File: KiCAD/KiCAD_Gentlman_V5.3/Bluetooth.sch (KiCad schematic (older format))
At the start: 16 parts, among them J7 PinHeader2.54mm_6, U7 nRF52832-QFAA, U8 nRF52832_DM-SModule, Y1 Y_32MHz

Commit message: KSG : 반이중통신용 회로도 구성 완료
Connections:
- net STM32_UART_TX is gone; now on net STM32_UART: J7.6 (Pin_6), U7.15 (P0.12), U8.22 (P0.12)
- net STM32_UART_RX renamed STM32_UART
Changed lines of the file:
@@
 	2300 3550 2050 3550
 Connection ~ 2300 3550
-Text GLabel 2200 4150 0    50   Input ~ 0
-nRF_SWCLK
 Wire Wire Line
 	2200 4150 3250 4150
-Text GLabel 2200 4250 0    50   Input ~ 0
+Text GLabel 2200 4250 0    50   BiDi ~ 0
 nRF_SWDIO
 Wire Wire Line
 	2200 4250 3250 4250
-Text GLabel 2200 4350 0    50   Input ~ 0
+Text GLabel 2200 4350 0    50   Output ~ 0
 nRF_UART_TX
 Wire Wire Line
@@
 	7100 2650 7500 2650
 Wire Wire Line
-	1300 7350 1450 7350
-Text GLabel 1450 7350 2    50   Input ~ 0
+	2450 6850 2750 6850
+Text GLabel 2750 6850 2    50   Input ~ 0
 DEC4
-NoConn ~ 1300 7350
+NoConn ~ 2450 6850
 NoConn ~ 5050 2350
 NoConn ~ 5050 2450
@@
 Wire Wire Line
 	1650 1650 2150 1650
-Text GLabel 2350 7050 2    50   Output ~ 0
+Text GLabel 2750 6550 2    50   Input ~ 0
 nRF_UART_TX
-Text GLabel 2350 7150 2    50   Output ~ 0
+Text GLabel 2750 6650 2    50   Output ~ 0
 nRF_UART_RX
-Text GLabel 1700 7150 0    50   Output ~ 0
-STM32_UART_TX
-Text GLabel 1700 7050 0    50   Output ~ 0
-STM32_UART_RX
-Wire Wire Line
-	1700 7050 2350 7050
-Wire Wire Line
-	1700 7150 2350 7150
+Text GLabel 2450 6550 0    50   BiDi ~ 0
+STM32_UART
+Wire Wire Line
+	2450 6550 2600 6550
+Text GLabel 2200 4150 0    50   Input ~ 0
+nRF_SWCLK
+Wire Wire Line
+	2600 6550 2600 6650
+Connection ~ 2600 6550
+Wire Wire Line
+	2600 6550 2750 6550
+Wire Wire Line
+	2600 6650 2750 6650
 $EndSCHEMATC

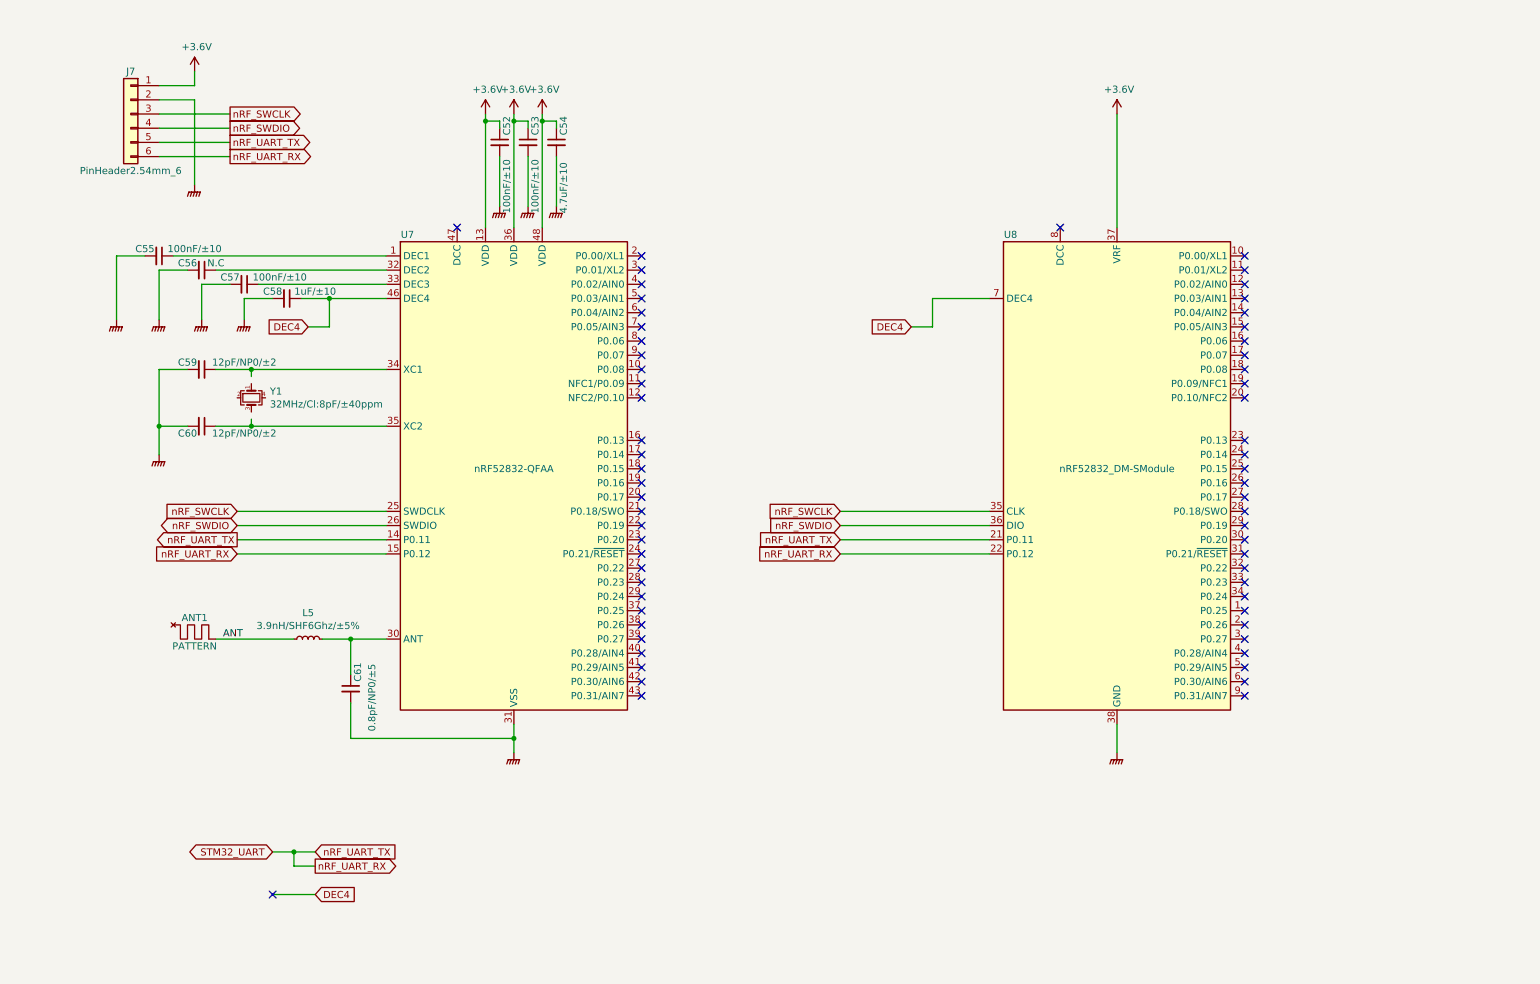
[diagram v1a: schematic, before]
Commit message: KSG : 회로도 에 nRF52 DC-DC 레귤레이터 추가
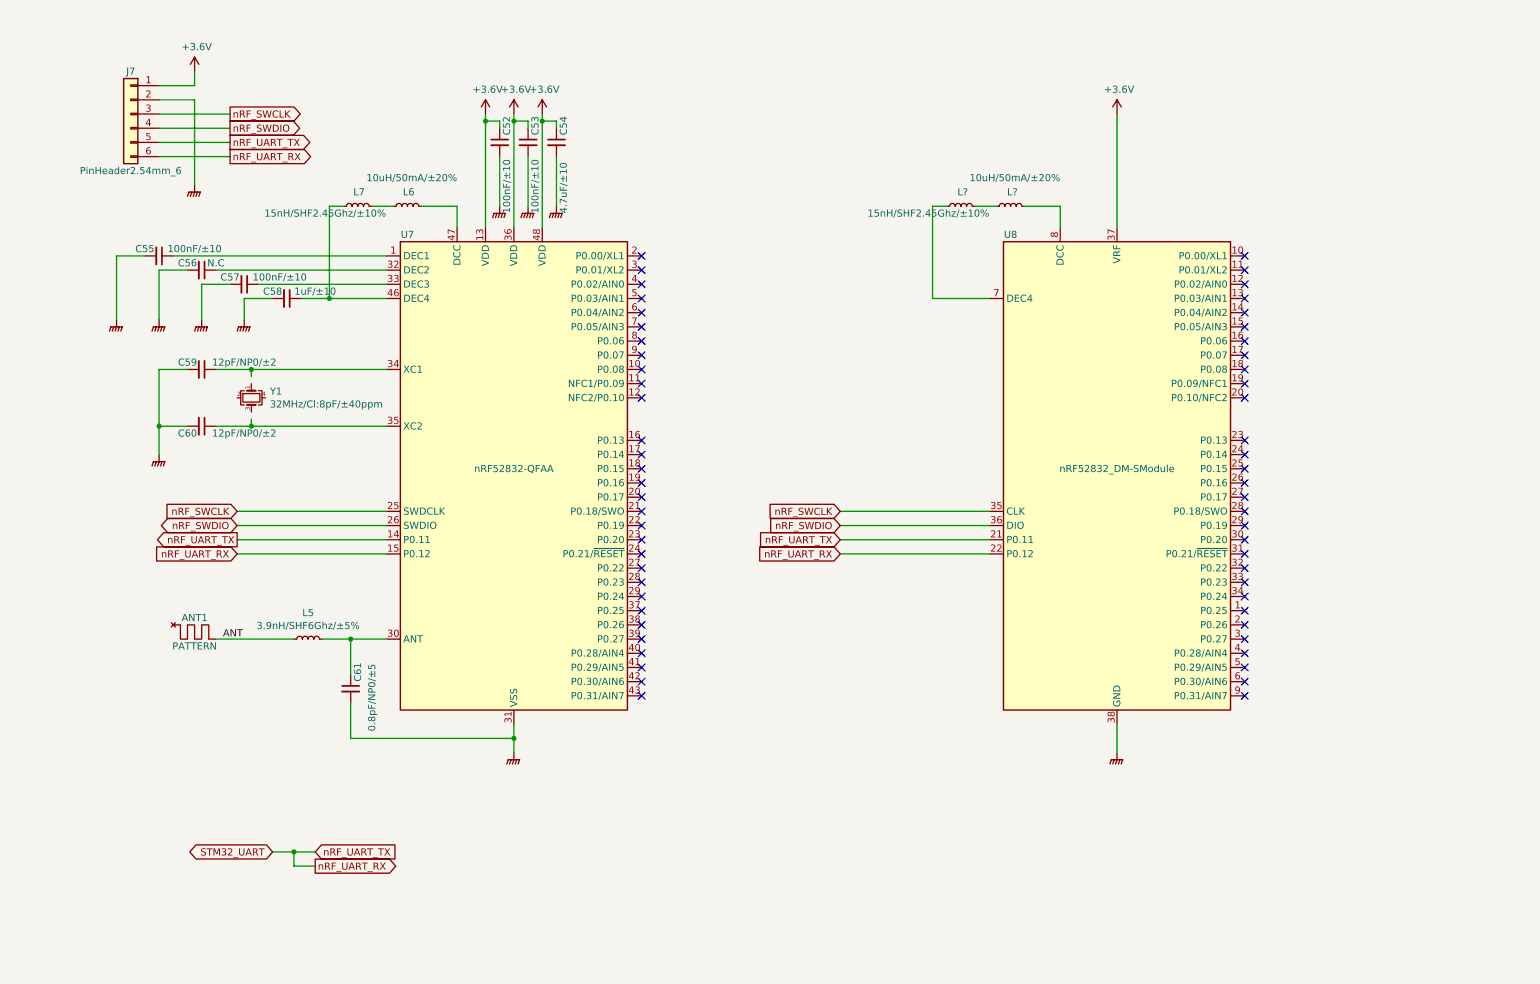
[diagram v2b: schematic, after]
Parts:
- added L6, L?: L_10uH, Custom:L_0603_1608Metric, symbol Custom:L_10uH
- added L7, L?: L_15nH, Custom:L_01005_0402Metric, symbol Custom:L_15nH
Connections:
- net at U7.47 (DCC): now also L6.2
- net at U8.8 (DCC): now also L?.2
- net DEC4: no longer names the net of C58.1, U7.46 (DEC4)
- net DEC4: now also L7.1; no longer U8.7 (DEC4)
- new net: L6.1, L7.2
- new net: L?.1, U8.7 (DEC4)
- new net: L?.1, L?.2
- no-connect marks 63 -> 60
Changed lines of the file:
@@
 Wire Wire Line
 	2250 2650 2450 2650
-Wire Wire Line
-	2650 2650 2850 2650
-Wire Wire Line
-	2850 2650 2850 2850
-Wire Wire Line
-	2850 2850 2700 2850
-Text GLabel 2700 2850 0    50   Input ~ 0
-DEC4
-Connection ~ 2850 2650
-Wire Wire Line
-	2850 2650 3250 2650
 $Comp
 L Custom:Y_32MHz Y1
@@
 Wire Wire Line
 	8400 1350 8400 2150
-NoConn ~ 8000 2150
-NoConn ~ 3750 2150
-Wire Wire Line
-	7100 2650 7100 2850
-Wire Wire Line
-	7100 2850 6950 2850
-Text GLabel 6950 2850 0    50   Input ~ 0
-DEC4
-Wire Wire Line
-	7100 2650 7500 2650
-Wire Wire Line
-	2450 6850 2750 6850
-Text GLabel 2750 6850 2    50   Input ~ 0
-DEC4
-NoConn ~ 2450 6850
 NoConn ~ 5050 2350
 NoConn ~ 5050 2450
@@
 Wire Wire Line
 	2600 6650 2750 6650
+$Comp
+L Custom:L_15nH L7
+U 1 1 61A0ACB5
+P 3050 2000
+F 0 "L7" V 3150 1950 50  0000 L CNN
+F 1 "L_15nH" H 3080 1960 50  0001 L CNN
+F 2 "Custom:L_01005_0402Metric" H 3050 2000 50  0001 C CNN
+F 3 ".\\Dataseets\\jti-cat-rf-ind-844822.pdf" H 3050 2000 50  0001 C CNN
+F 4 "15nH/SHF2.45Ghz/±10%" V 3000 1800 50  0000 L CNN "Field4"
+F 5 "SMD INDUCTOR" H 3050 2000 50  0001 C CNN "Description"
+F 6 "15nH/SHF21Ghz/±10%" H 3050 2000 50  0001 C CNN "Comment"
+F 7 "1005" H 3050 2000 50  0001 C CNN "TYPE"
+F 8 "JOHANSON" H 3050 2000 50  0001 C CNN "MAKER"
+F 9 "L-07C15NKV6T" H 3050 2000 50  0001 C CNN "PartName"
+F 10 "https://kr.mouser.com/ProductDetail/Johanson/L-07C15NKV6T?qs=sGAEpiMZZMsjJi7B1kCaqYmWy2J2VjPA6p6zKg5MyIw%3D" H 3050 2000 50  0001 C CNN "Shop"
+	1    3050 2000
+	0    -1   -1   0
+$EndComp
+$Comp
+L Custom:L_10uH L6
+U 1 1 61A09931
+P 3400 2000
+F 0 "L6" V 3500 1950 50  0000 L CNN
+F 1 "L_10uH" H 3430 1960 50  0001 L CNN
+F 2 "Custom:L_0603_1608Metric" H 3400 2000 50  0001 C CNN
+F 3 ".\\Dataseets\\JELF243B_0012-1633801.pdf" H 3400 2000 50  0001 C CNN
+F 4 "10uH/50mA/±20%" V 3600 1650 50  0000 L CNN "Field4"
+F 5 "SMD INDUCTOR" H 3400 2000 50  0001 C CNN "Description"
+F 6 "10uH/50mA/±20%" H 3400 2000 50  0001 C CNN "Comment"
+F 7 "0603" H 3400 2000 50  0001 C CNN "TYPE"
+F 8 "MURATA" H 3400 2000 50  0001 C CNN "MAKER"
+F 9 "LQM18FN100M00D" H 3400 2000 50  0001 C CNN "PartName"
+F 10 "https://kr.mouser.com/ProductDetail/Murata/LQM18FN100M00D?qs=sGAEpiMZZMvxX9Q80wbhCb2WlNhDJeZC" H 3400 2000 50  0001 C CNN "Shop"
+	1    3400 2000
+	0    -1   -1   0
+$EndComp
+Wire Wire Line
+	2950 2000 2850 2000
+Wire Wire Line
+	3150 2000 3300 2000
+Wire Wire Line
+	3500 2000 3750 2000
+Wire Wire Line
+	3750 2000 3750 2150
+Wire Wire Line
+	2650 2650 2850 2650
+Wire Wire Line
+	2850 2000 2850 2650
+Connection ~ 2850 2650
+Wire Wire Line
+	2850 2650 3250 2650
+$Comp
+L Custom:L_15nH L?
+U 1 1 61A6256C
+P 7300 2000
+F 0 "L?" V 7400 1950 50  0000 L CNN
+F 1 "L_15nH" H 7330 1960 50  0001 L CNN
+F 2 "Custom:L_01005_0402Metric" H 7300 2000 50  0001 C CNN
+F 3 ".\\Dataseets\\jti-cat-rf-ind-844822.pdf" H 7300 2000 50  0001 C CNN
+F 4 "15nH/SHF2.45Ghz/±10%" V 7250 1800 50  0000 L CNN "Field4"
+F 5 "SMD INDUCTOR" H 7300 2000 50  0001 C CNN "Description"
+F 6 "15nH/SHF21Ghz/±10%" H 7300 2000 50  0001 C CNN "Comment"
+F 7 "1005" H 7300 2000 50  0001 C CNN "TYPE"
+F 8 "JOHANSON" H 7300 2000 50  0001 C CNN "MAKER"
+F 9 "L-07C15NKV6T" H 7300 2000 50  0001 C CNN "PartName"
+F 10 "https://kr.mouser.com/ProductDetail/Johanson/L-07C15NKV6T?qs=sGAEpiMZZMsjJi7B1kCaqYmWy2J2VjPA6p6zKg5MyIw%3D" H 7300 2000 50  0001 C CNN "Shop"
+	1    7300 2000
+	0    -1   -1   0
+$EndComp
+$Comp
+L Custom:L_10uH L?
+U 1 1 61A62579
+P 7650 2000
+F 0 "L?" V 7750 1950 50  0000 L CNN
+F 1 "L_10uH" H 7680 1960 50  0001 L CNN
+F 2 "Custom:L_0603_1608Metric" H 7650 2000 50  0001 C CNN
+F 3 ".\\Dataseets\\JELF243B_0012-1633801.pdf" H 7650 2000 50  0001 C CNN
+F 4 "10uH/50mA/±20%" V 7850 1650 50  0000 L CNN "Field4"
+F 5 "SMD INDUCTOR" H 7650 2000 50  0001 C CNN "Description"
+F 6 "10uH/50mA/±20%" H 7650 2000 50  0001 C CNN "Comment"
+F 7 "0603" H 7650 2000 50  0001 C CNN "TYPE"
+F 8 "MURATA" H 7650 2000 50  0001 C CNN "MAKER"
+F 9 "LQM18FN100M00D" H 7650 2000 50  0001 C CNN "PartName"
+F 10 "https://kr.mouser.com/ProductDetail/Murata/LQM18FN100M00D?qs=sGAEpiMZZMvxX9Q80wbhCb2WlNhDJeZC" H 7650 2000 50  0001 C CNN "Shop"
+	1    7650 2000
+	0    -1   -1   0
+$EndComp
+Wire Wire Line
+	7200 2000 7100 2000
+Wire Wire Line
+	7400 2000 7550 2000
+Wire Wire Line
+	7750 2000 8000 2000
+Wire Wire Line
+	8000 2000 8000 2150
+Wire Wire Line
+	7100 2000 7100 2650
+Wire Wire Line
+	7100 2650 7500 2650
 $EndSCHEMATC

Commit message: KSG : V5.3B용으로 회로도 수정 및 PCB 아트웤 완료.(샘플PCB주문됨)
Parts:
- added JP1, JP2, JP3: PinHeader2.54mm-2-Jumper, Custom:PinHeader_1x02_P2.54mm_Vertical, symbol Custom:PinHeader2.54mm-2-Jumper
- added L10: L_10uH, Custom:L_0603_1608Metric, symbol Custom:L_10uH
- added L11: L_15nH, Custom:L_0402_1005Metric, symbol Custom:L_15nH
- added U9: nRF52810_PLE52M, Custom:nRF52810_PLE52M, symbol Custom:nRF52810_PLE52M
- ANT1: symbol Custom:ANT -> Custom:PATTERN_ANT; Field4 PATTERN -> (none)
- C52, C53, C55, C57: Comment 100nF/±10 -> (none); Description CHIP CERAMIC CAP -> (none); Field4 100nF/±10 -> (none); MAKER MURATA ELECTRONICS -> (none); Maker (none) -> SAMSUNG ELECTRO-MECHANICS; PartName GRM155R61H104KE14D -> 100nF/±10; Replacement (none) -> CL05A104KA5NNNC; Shop https://kr.mouser.com/ProductDetail/Murata/GRM155R61H104KE1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 -> https://www.eleparts.co.kr/goods/view?no=8011439; TYPE 1005 -> (none); Type (none) -> CHIP CERAMIC CAP
- C54: Comment 4.7uF/±10 -> (none); Description CHIP CERAMIC CAP -> (none); Field4 4.7uF/±10 -> (none); MAKER SAMSUNG ELECTRO-MECHANICS -> (none); Maker (none) -> SAMSUNG ELECTRO-MECHANICS; PartName CL05A475KQ5NRNC -> 4.7uF/±10; Replacement (none) -> CL05A475KP5NRNC; Shop https://kr.mouser.com/ProductDetail/Samsung-Electro-Mechani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 -> https://www.eleparts.co.kr/goods/view?no=8057798; TYPE 1005 -> (none); Type (none) -> CHIP CERAMIC CAP
- C56: Comment N.C -> (none); Description CHIP CERAMIC CAP -> (none); Field4 N.C -> (none); MAKER MURATA ELECTRONICS -> (none); PartName (none) -> N.C; TYPE 1005 -> (none); Type (none) -> CHIP CERAMIC CAP
- C58: Comment 1uF/±10 -> (none); Description CHIP CERAMIC CAP -> (none); Field4 1uF/±10 -> (none); MAKER SAMSUNG ELECTRO-MECHANICS -> (none); Maker (none) -> SAMSUNG ELECTRO-MECHANICS; PartName CL05A105KP5NNWC -> 1uF/±10; Replacement (none) -> CL05A105KA5NQNC; Shop https://kr.mouser.com/ProductDetail/Samsung-Electro-Mechani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 -> https://www.eleparts.co.kr/goods/view?no=8010445; TYPE 1005 -> (none); Type (none) -> CHIP CERAMIC CAP
- C59, C60: Comment 12pF/NP0/±2 -> (none); Description CHIP CERAMIC CAP -> (none); Field4 12pF/NP0/±2 -> (none); MAKER MURATA ELECTRONICS -> (none); Maker (none) -> WALSIN; PartName GRM1555C1H120GA01D -> 12pF/NP0/±2; Replacement (none) -> 0402N120G250CT; Shop https://kr.mouser.com/ProductDetail/Murata/GRM1555C1H120GA0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 -> https://www.eleparts.co.kr/goods/view?no=9226620; TYPE 1005 -> (none); Type (none) -> CHIP CERAMIC CAP
- C61: Comment 0.8pF/NP0/±5 -> (none); Description CHIP CERAMIC CAP -> (none); Field4 0.8pF/NP0/±5 -> (none); MAKER MURATA ELECTRONICS -> (none); Maker (none) -> MURATA; PartName GRM1555C1HR80WA01D -> 0.8pF/NP0/±5; Replacement (none) -> GRM1555C1HR80WA01D; Shop https://kr.mouser.com/ProductDetail/Murata/GRM1555C1HR80WA0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 -> https://www.eleparts.co.kr/goods/view?no=9591919; TYPE 1005 -> (none); Type (none) -> CHIP CERAMIC CAP
- J7: value PinHeader2.54mm_6 -> PinHeader2.54mm_5; footprint Custom:PinHeader_1x06_P2.54mm_Vertical -> Custom:PinHeader_1x05_P2.54mm_Vertical; symbol Custom:PinHeader2.54mm_6 -> Custom:PinHeader2.54mm_5; Comment PinHeader2.54mm-6P -> (none); Description PIN HEADER -> (none); PartName (none) -> PinHeader2.54mm-5P; TYPE DIP-6 -> (none); Type (none) -> PIN HEADER
- L5: footprint Custom:L_01005_0402Metric -> Custom:L_0402_1005Metric; Comment 3.9nH/SHF6Ghz/±5% -> (none); Description SMD INDUCTOR -> (none); Field4 3.9nH/SHF6Ghz/±5% -> (none); MAKER SUHKWANG -> (none); Maker (none) -> MURATA; PartName 7447840039G -> 3.9nH/SHF6Ghz/±5%; Replacement (none) -> LQG15HS3N9C02D; Shop https://kr.mouser.com/ProductDetail/Wurth-Elektronik/744784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 -> https://www.eleparts.co.kr/goods/view?no=9578079; TYPE 1005 -> (none); Type (none) -> SMD INDUCTOR
- L6: Comment 10uH/50mA/±20% -> (none); Description SMD INDUCTOR -> (none); Field4 10uH/50mA/±20% -> (none); MAKER MURATA -> (none); Maker (none) -> MURATA; PartName LQM18FN100M00D -> 10uH/50mA/±20%; Replacement (none) -> LQM18FN100M00D; Shop https://kr.mouser.com/ProductDetail/Murata/LQM18FN100M00D?q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 -> https://www.eleparts.co.kr/goods/view?no=7457243; TYPE 0603 -> (none); Type (none) -> SMD INDUCTOR
- L7: footprint Custom:L_01005_0402Metric -> Custom:L_0402_1005Metric; Comment 15nH/SHF21Ghz/±10% -> (none); Description SMD INDUCTOR -> (none); Field4 15nH/SHF2.45Ghz/±10% -> (none); MAKER JOHANSON -> (none); Maker (none) -> MURATA; PartName L-07C15NKV6T -> 15nH/SHF2.45Ghz/±10%; Replacement (none) -> LQG15HS15NJ02D; Shop https://kr.mouser.com/ProductDetail/Johanson/L-07C15NKV6T?q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 -> https://www.eleparts.co.kr/goods/view?no=6591752; TYPE 1005 -> (none); Type (none) -> SMD INDUCTOR
- L8: renamed from L?; Comment 10uH/50mA/±20% -> (none); Description SMD INDUCTOR -> (none); Field4 10uH/50mA/±20% -> (none); MAKER MURATA -> (none); Maker (none) -> MURATA; PartName LQM18FN100M00D -> 10uH/50mA/±20%; Replacement (none) -> LQM18FN100M00D; Shop https://kr.mouser.com/ProductDetail/Murata/LQM18FN100M00D?q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 -> https://www.eleparts.co.kr/goods/view?no=7457243; TYPE 0603 -> (none); Type (none) -> SMD INDUCTOR
- L9: renamed from L?; footprint Custom:L_01005_0402Metric -> Custom:L_0402_1005Metric; Comment 15nH/SHF21Ghz/±10% -> (none); Description SMD INDUCTOR -> (none); Field4 15nH/SHF2.45Ghz/±10% -> (none); MAKER JOHANSON -> (none); Maker (none) -> MURATA; PartName L-07C15NKV6T -> 15nH/SHF2.45Ghz/±10%; Replacement (none) -> LQG15HS15NJ02D; Shop https://kr.mouser.com/ProductDetail/Johanson/L-07C15NKV6T?q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 -> https://www.eleparts.co.kr/goods/view?no=6591752; TYPE 1005 -> (none); Type (none) -> SMD INDUCTOR
- U7: Comment nRF52832-QFAA -> (none); Description SMD MCU -> (none); MAKER NORDIC SEMICONDUCTOR -> (none); Maker (none) -> NORDIC SEMICONDUCTOR; Shop https://www.devicemart.co.kr/goods/view?no=10901051 -> https://smartstore.naver.com/ifcompany/products/4967647336?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; TYPE QFN-48 -> (none); Type (none) -> SMD MCU
- U8: Comment nRF52832_DM-SModule -> (none); Description SMD BLE MODULE -> (none); MAKER NORDIC SEMICONDUCTOR -> (none); Maker (none) -> DMTECK; TYPE nRF52832_DM-SModule -> (none); Type (none) -> SMD BLE MODULE
- Y1: Comment 32MHz/Cl:8pF/±40ppm -> (none); Description SMD CRYSTAL -> (none); Field4 32MHz/Cl:8pF/±40ppm -> (none); MAKER ECS -> (none); Maker (none) -> Yangxing Tech; PartName ECS-320-8-37B-7KM-TR -> 32MHz/Cl:8pF/±40ppm; Replacement (none) -> X201632MKD4SI; Shop https://kr.mouser.com/ProductDetail/ECS/ECS-320-8-37B-7KM-T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 -> https://www.eleparts.co.kr/goods/view?no=6614084; TYPE 2016 -> (none); Type (none) -> SMD CRYSTAL
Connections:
- net labels added: UART
- net labels removed: STM32_UART, nRF_UART_RX, nRF_UART_TX
- wire segments 79 -> 101
- no-connect marks 60 -> 90
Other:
- moved on the sheet: ANT1, C52, C53, C54, C55, C56, C57, C58, C59, C60, C61, L5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
